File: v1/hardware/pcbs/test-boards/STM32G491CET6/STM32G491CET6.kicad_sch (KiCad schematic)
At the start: 45 parts, among them J1 Conn_02x10_Odd_Even, J2 Conn_02x10_Odd_Even, J3 Conn_01x04, U1 STM32G491CETx, Y1 Crystal_GND24, Y2 Crystal

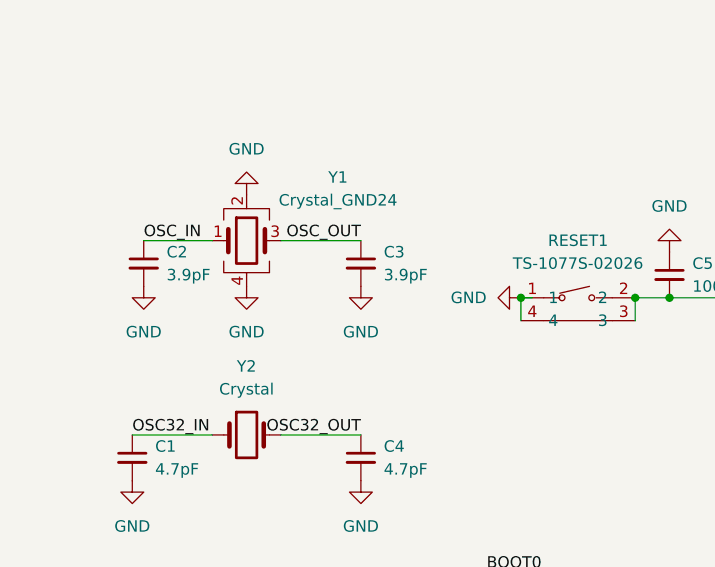
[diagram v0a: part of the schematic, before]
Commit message: lcsc numbers for crystals
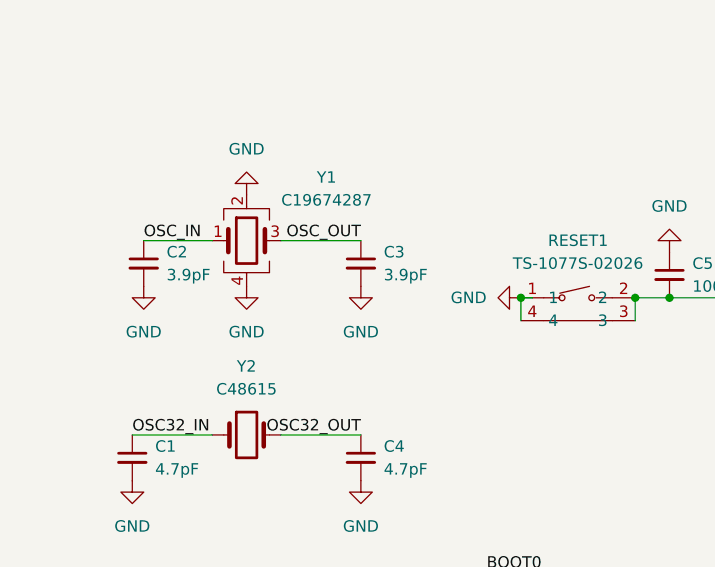
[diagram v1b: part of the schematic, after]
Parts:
- Y1: value Crystal_GND24 -> C19674287
- Y2: value Crystal -> C48615
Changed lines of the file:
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@@
 		(fields_autoplaced yes)
 		(property "Reference" "Y1"
-			(at 52.07 53.9339 0)
+			(at 50.8 53.9339 0)
 			(effects
 				(font
@@
 			)
 		)
-		(property "Value" "Crystal_GND24"
-			(at 52.07 56.4739 0)
+		(property "Value" "C19674287"
+			(at 50.8 56.4739 0)
 			(effects
 				(font
@@
 			)
 		)
-		(property "Value" "Crystal"
+		(property "Value" "C48615"
 			(at 41.91 77.47 0)
 			(effects

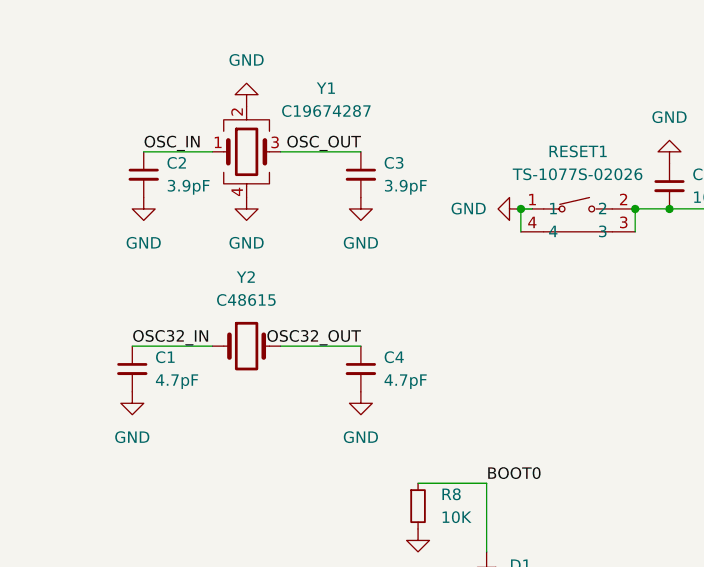
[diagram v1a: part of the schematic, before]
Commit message: new FOC driver schematic
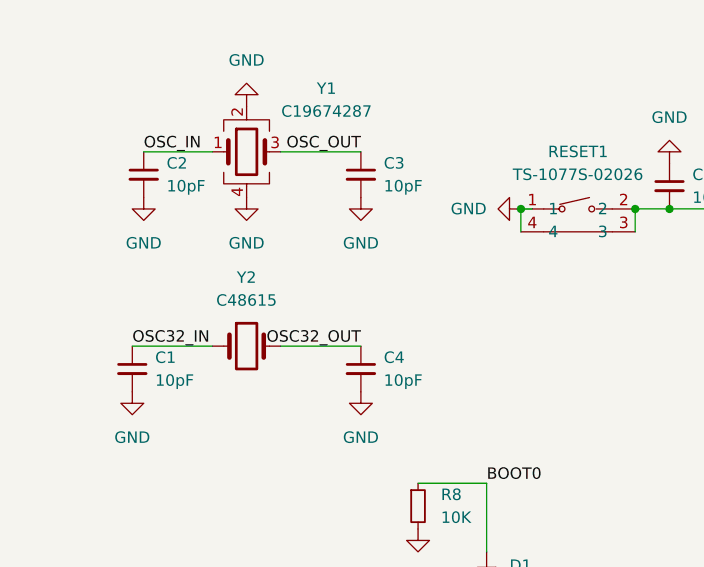
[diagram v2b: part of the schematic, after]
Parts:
- BOOT1: symbol EasyEDA:TS-1077S-02026 -> symbols:TS-1077S-02026
- C1, C4: value 4.7pF -> 10pF; symbol Device:C_Small -> symbols:C_Small
- C10, C11, C12, C13, C14, C5, C6, C7, C8, C9: symbol Device:C_Small -> symbols:C_Small
- C2, C3: value 3.9pF -> 10pF; symbol Device:C_Small -> symbols:C_Small
- D1, D2, D3: symbol Device:D_Schottky_Small -> symbols:D_Schottky_Small
- D4, D5: symbol Device:D_TVS -> symbols:D_TVS
- FB1: symbol Device:FerriteBead_Small -> symbols:FerriteBead_Small
- H1, H2, H3: symbol Mechanical:MountingHole_Pad -> symbols:MountingHole_Pad
- J1, J2: symbol Connector_Generic:Conn_02x10_Odd_Even -> symbols:Conn_02x10_Odd_Even
- J3: symbol Connector_Generic:Conn_01x04 -> symbols:Conn_01x04
- LDO1: symbol Regulator_Linear:ME6211C33M5 -> symbols:ME6211C33M5
- LED1, LED2: symbol Device:LED -> symbols:LED
- R1, R9: symbol Device:R -> symbols:R
- R2, R3, R4, R5, R6, R7, R8: symbol Device:R_Small -> symbols:R_Small
- RESET1: symbol EasyEDA:TS-1077S-02026 -> symbols:TS-1077S-02026_1
- U1: symbol MCU_ST_STM32G4:STM32G491CETx -> symbols:STM32G491CETx
- USB1: symbol EasyEDA:TYPE-C16PIN2MD(073) -> symbols:TYPE-C16PIN2MD(073)
- USBPWR1: symbol Jumper:Jumper_2_Bridged -> symbols:Jumper_2_Bridged
- Y1: symbol Device:Crystal_GND24 -> symbols:Crystal_GND24
- Y2: symbol Device:Crystal -> symbols:Crystal
